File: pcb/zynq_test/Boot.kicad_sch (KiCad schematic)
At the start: 9 parts, among them J901 A-MicroTF-1.85A, U901 LSF0108PWR, U902 MT25QL01GBBB8ESF-0SIT

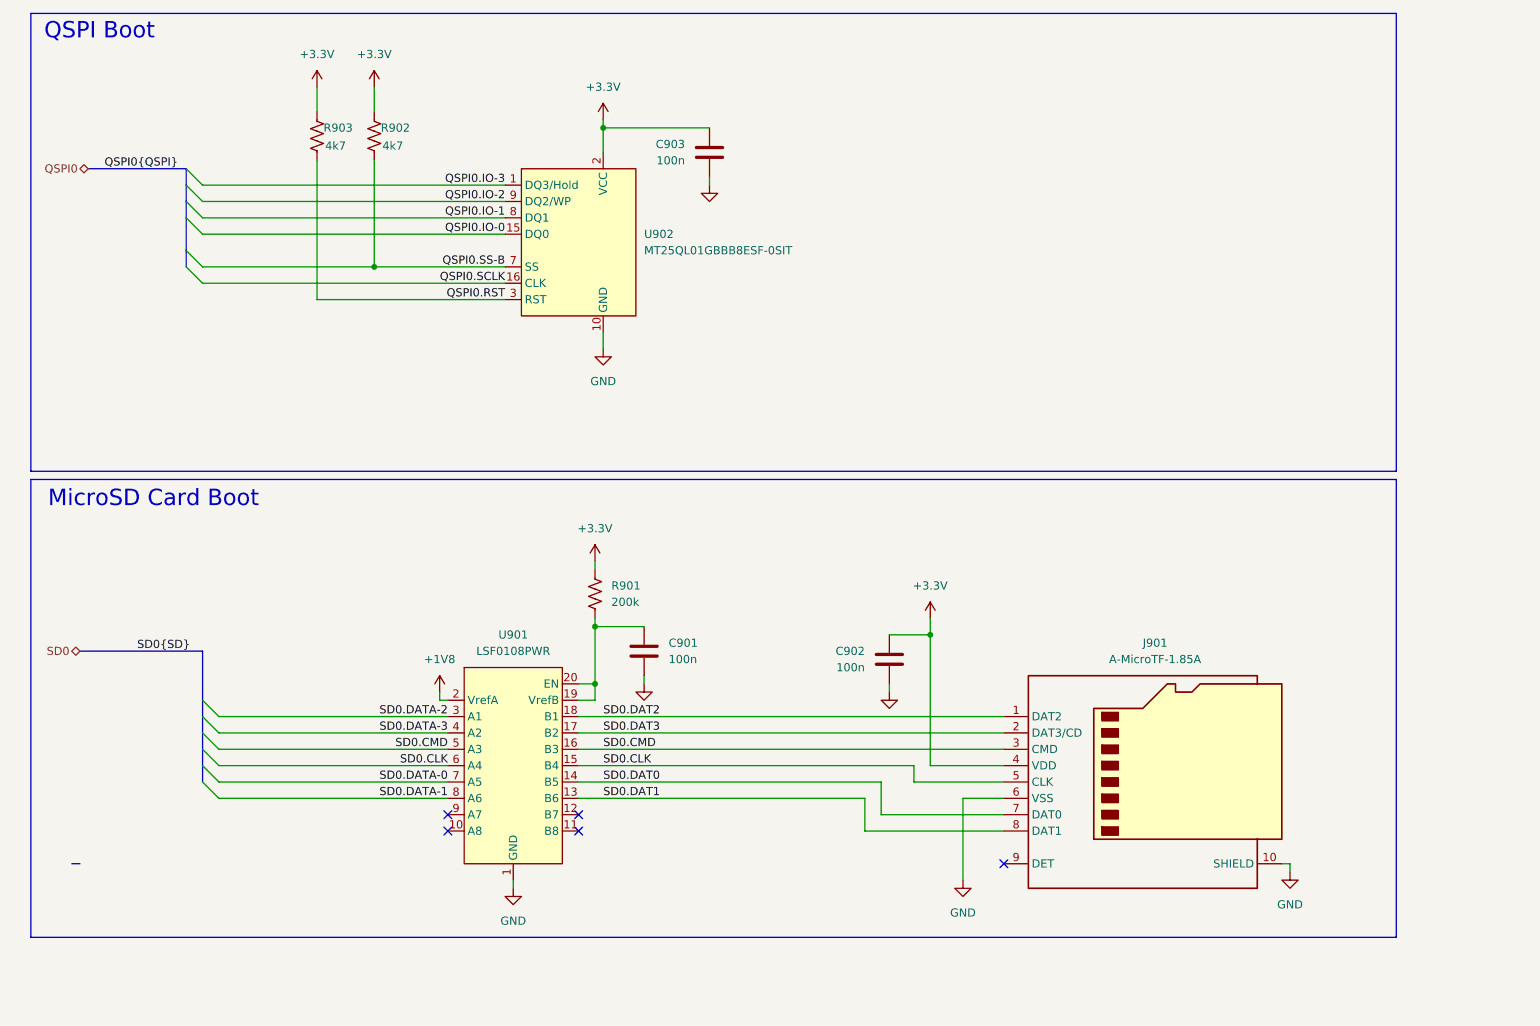
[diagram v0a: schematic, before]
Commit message: Added Cameras, changed SD card IC for skew reasons
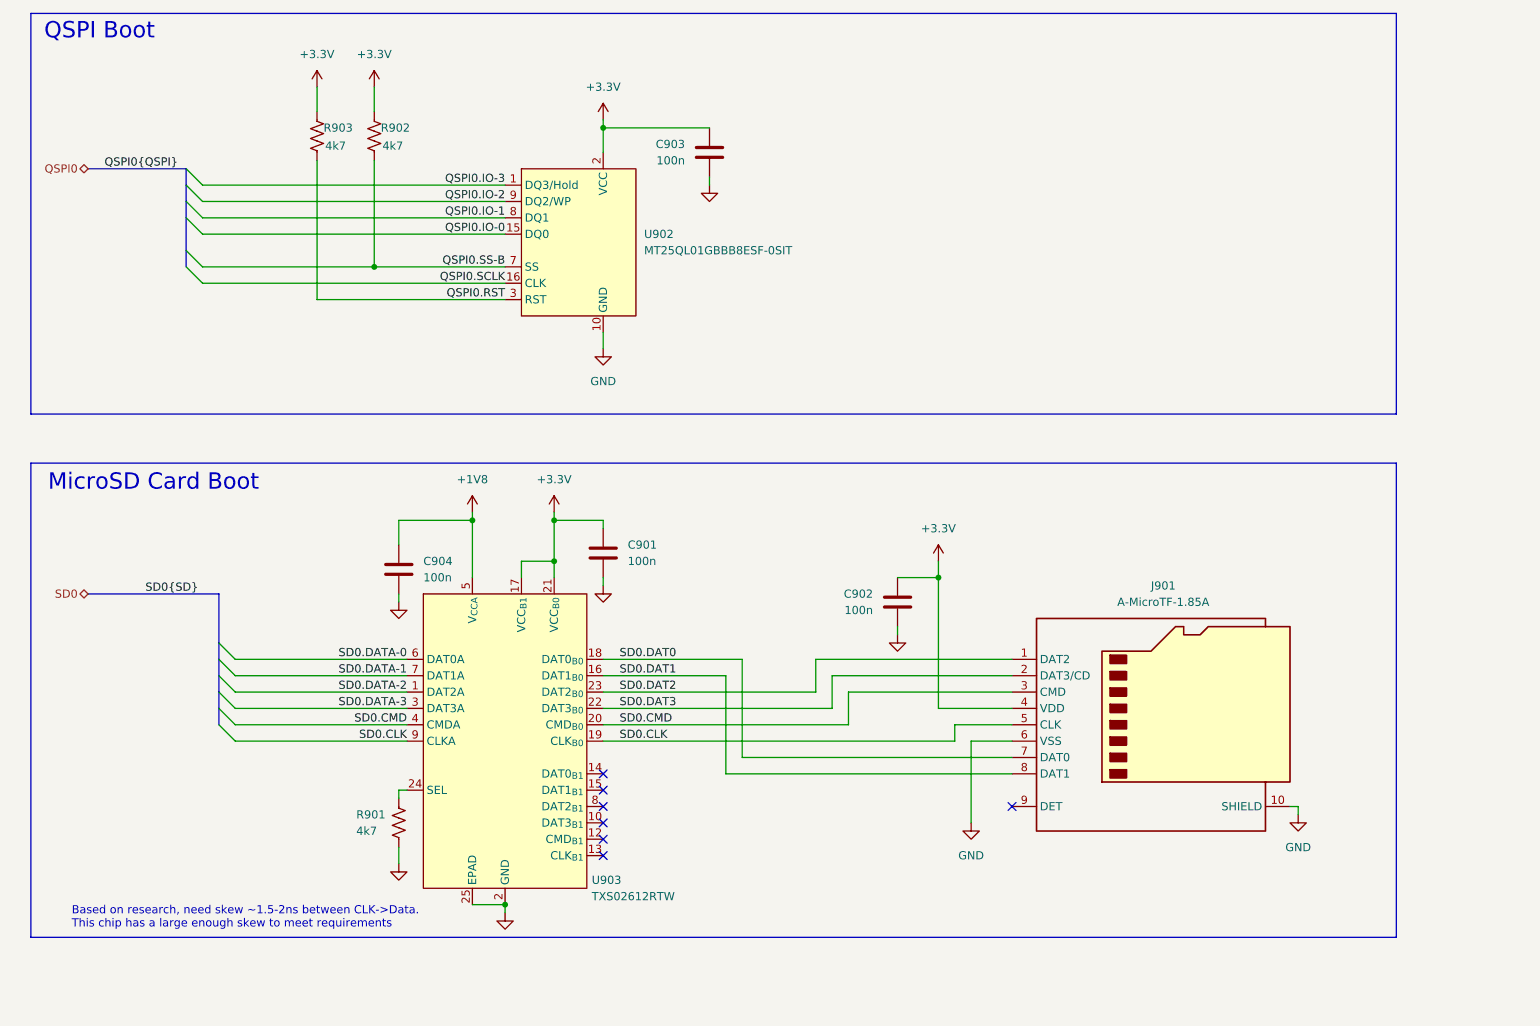
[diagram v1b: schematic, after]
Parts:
- removed U901: LSF0108PWR, symbol other:LSF0108PWR
- added C904: 100n, symbol Device:C
- added U903: TXS02612RTW, Package_DFN_QFN:WQFN-24-1EP_4x4mm_P0.5mm_EP2.45x2.45mm_ThermalVias, symbol Logic_LevelTranslator:TXS02612RTW
- R901: value 200k -> 4k7
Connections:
- net +1V8: now also C904.1, U903.5 (V_{CCA})
- net +3.3V: now also C901.1, U903.17 (VCC_{B1}), U903.21 (VCC_{B0}); no longer R901.1
- net GND: now also R901.2, C904.2, U903.11 (GND), U903.2 (GND), U903.25 (EPAD)
- net SD0.CLK: now also U903.19 (CLK_{B0}), U903.9 (CLKA)
- net SD0.CMD: now also U903.20 (CMD_{B0}), U903.4 (CMDA)
- net SD0.DAT0: now also U903.18 (DAT0_{B0})
- net SD0.DAT1: now also U903.16 (DAT1_{B0})
- net SD0.DAT2: now also U903.23 (DAT2_{B0})
- net SD0.DAT3: now also U903.22 (DAT3_{B0})
- net SD0.DATA-0: now also U903.6 (DAT0A)
- net SD0.DATA-1: now also U903.7 (DAT1A)
- net SD0.DATA-2: now also U903.1 (DAT2A)
- net SD0.DATA-3: now also U903.3 (DAT3A)
- new net: R901.1, U903.24 (SEL)
- no-connect marks 5 -> 7
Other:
- note added: "Based on research, need skew ~1.5-2ns between CLK->Data. This chip has a large enough skew to meet requirements"
- moved on the sheet: C901, C902, J901

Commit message: Finished HDMI
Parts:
- J901: footprint (none) -> Connector_Card:microSD_HC_Molex_47219-2001
- U903: footprint Package_DFN_QFN:WQFN-24-1EP_4x4mm_P0.5mm_EP2.45x2.45mm_ThermalVias -> Package_DFN_QFN:WQFN-24-1EP_4x4mm_P0.5mm_EP2.45x2.45mm
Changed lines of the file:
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@@
 			)
 		)
-		(property "Footprint" "Package_DFN_QFN:WQFN-24-1EP_4x4mm_P0.5mm_EP2.45x2.45mm_ThermalVias"
+		(property "Footprint" "Package_DFN_QFN:WQFN-24-1EP_4x4mm_P0.5mm_EP2.45x2.45mm"
 			(at 104.14 170.18 0)
 			(effects
@@
 			)
 		)
-		(property "Footprint" ""
+		(property "Footprint" "Connector_Card:microSD_HC_Molex_47219-2001"
 			(at 257.81 114.3 0)
 			(effects
